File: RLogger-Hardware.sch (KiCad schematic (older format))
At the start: 13 parts

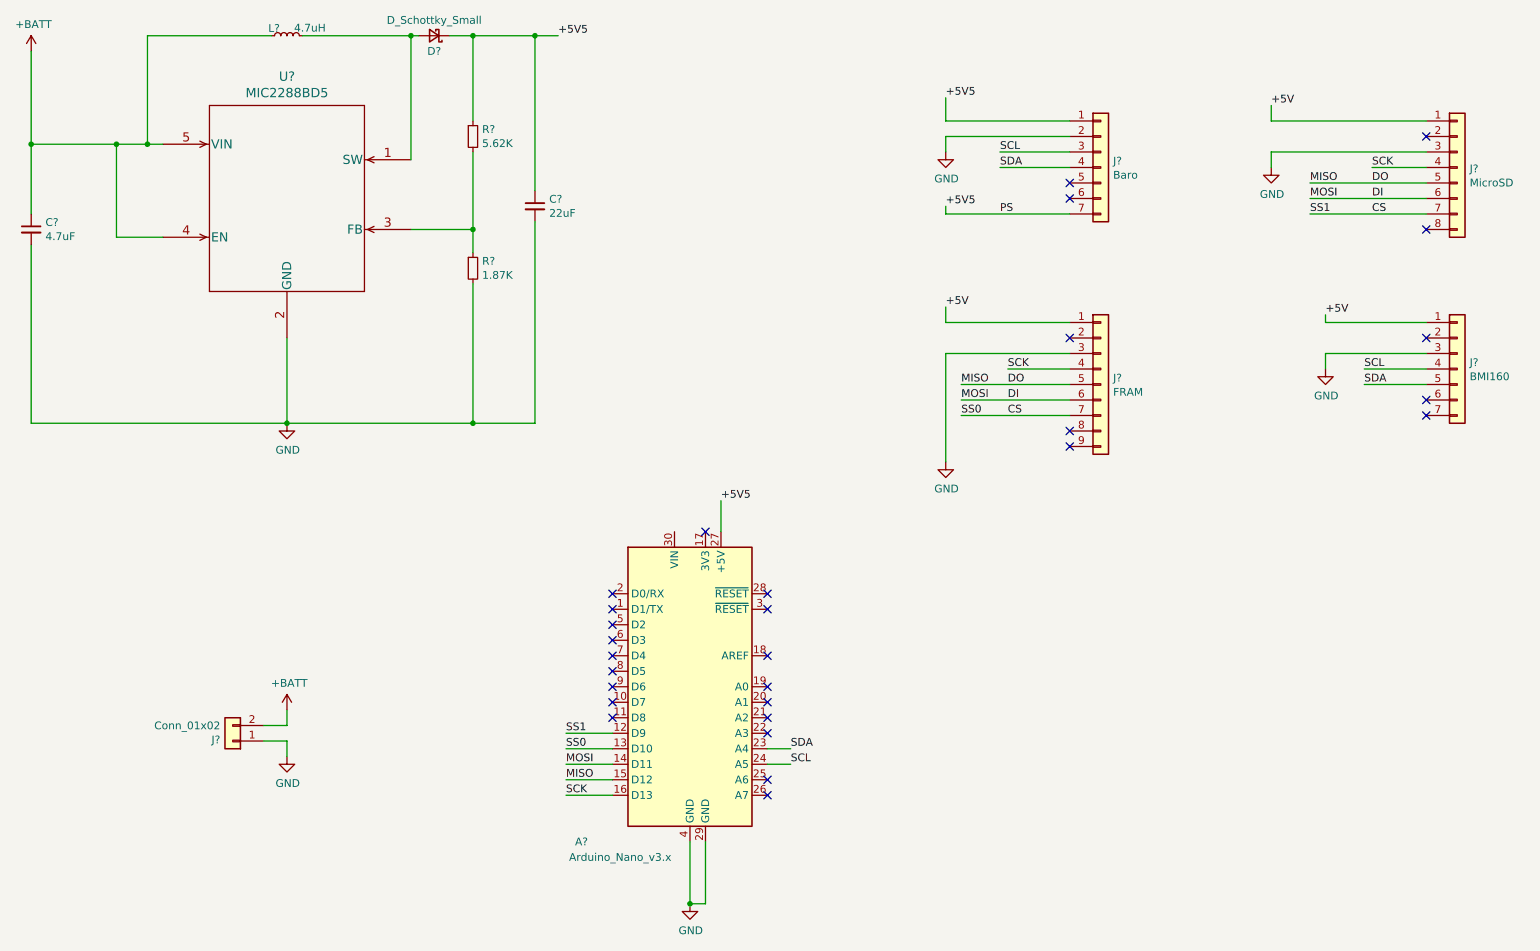
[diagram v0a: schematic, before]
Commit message: Assigned footprints.
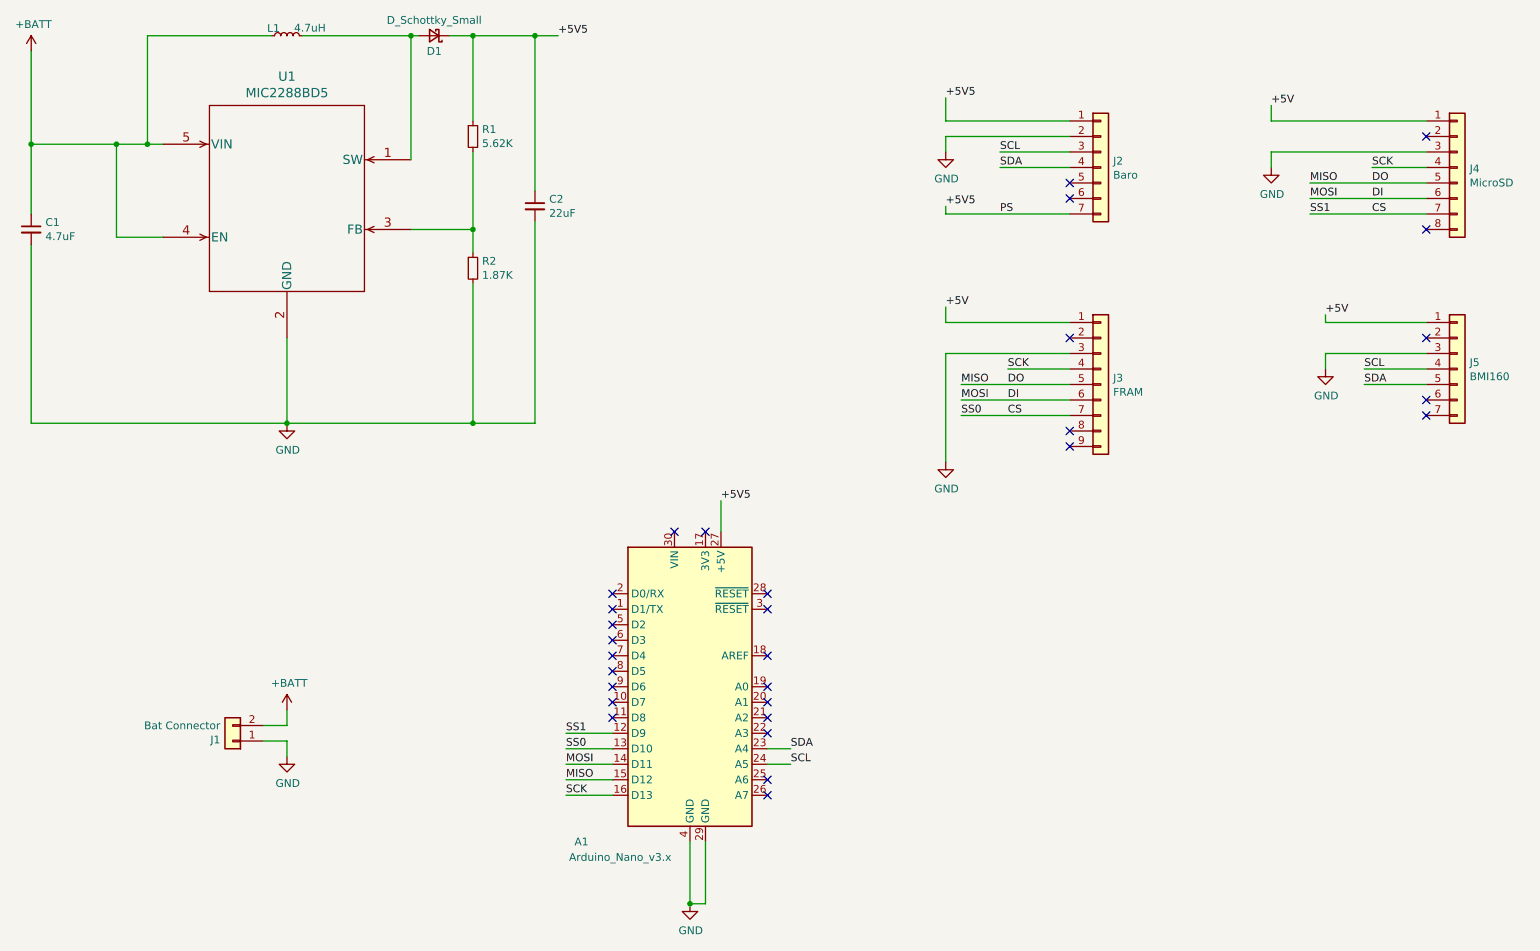
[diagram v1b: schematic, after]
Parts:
- C1: renamed from C?; footprint (none) -> Capacitor_SMD:C_0805_2012Metric_Pad1.15x1.40mm_HandSolder
- C2: renamed from C?; footprint (none) -> Capacitor_SMD:C_1206_3216Metric_Pad1.33x1.80mm_HandSolder
- D1: renamed from D?; footprint (none) -> Diode_SMD:D_Powermite_AK
- J1: renamed from J?; value Conn_01x02 -> Bat Connector; footprint (none) -> Connector_PinSocket_2.54mm:PinSocket_1x02_P2.54mm_Vertical
- J2, J5: renamed from J?; footprint (none) -> Connector_PinSocket_2.54mm:PinSocket_1x07_P2.54mm_Vertical
- J3: renamed from J?; footprint (none) -> Connector_PinSocket_2.54mm:PinSocket_1x09_P2.54mm_Vertical
- J4: renamed from J?; footprint (none) -> Connector_PinSocket_2.54mm:PinSocket_1x08_P2.54mm_Vertical
- L1: renamed from L?; footprint (none) -> Inductor_SMD:L_0805_2012Metric_Pad1.05x1.20mm_HandSolder
- R1, R2: renamed from R?; footprint (none) -> Resistor_SMD:R_0805_2012Metric_Pad1.15x1.40mm_HandSolder
- U1: renamed from U?; footprint TSOT-23-5_D5_MCL -> Package_TO_SOT_SMD:SOT-23-5_HandSoldering
- gave numbers to parts that had none: 1
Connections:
- no-connect marks 29 -> 30
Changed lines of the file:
@@
 $EndDescr
 $Comp
-L MCU_Module:Arduino_Nano_v3.x A?
+L MCU_Module:Arduino_Nano_v3.x A1
 U 1 1 6083FCEE
 P 5150 5000
-F 0 "A?" H 4450 4000 50  0000 C CNN
+F 0 "A1" H 4450 4000 50  0000 C CNN
 F 1 "Arduino_Nano_v3.x" H 4700 3900 50  0000 C CNN
 F 2 "Module:Arduino_Nano" H 5150 5000 50  0001 C CIN
@@
 $EndComp
 $Comp
-L Connector_Generic:Conn_01x08 J?
+L Connector_Generic:Conn_01x08 J4
 U 1 1 60843AEA
 P 10100 1650
-F 0 "J?" H 10180 1642 50  0000 L CNN
+F 0 "J4" H 10180 1642 50  0000 L CNN
 F 1 "MicroSD" H 10180 1551 50  0000 L CNN
-F 2 "" H 10100 1650 50  0001 C CNN
+F 2 "Connector_PinSocket_2.54mm:PinSocket_1x08_P2.54mm_Vertical" H 10100 1650 50  0001 C CNN
 F 3 "~" H 10100 1650 50  0001 C CNN
 	1    10100 1650
@@
 $EndComp
 $Comp
-L Connector_Generic:Conn_01x07 J?
+L Connector_Generic:Conn_01x07 J5
 U 1 1 6084440D
 P 10100 2950
-F 0 "J?" H 10180 2992 50  0000 L CNN
+F 0 "J5" H 10180 2992 50  0000 L CNN
 F 1 "BMI160" H 10180 2901 50  0000 L CNN
-F 2 "" H 10100 2950 50  0001 C CNN
+F 2 "Connector_PinSocket_2.54mm:PinSocket_1x07_P2.54mm_Vertical" H 10100 2950 50  0001 C CNN
 F 3 "~" H 10100 2950 50  0001 C CNN
 	1    10100 2950
@@
 $EndComp
 $Comp
-L Connector_Generic:Conn_01x07 J?
+L Connector_Generic:Conn_01x07 J2
 U 1 1 60844CC8
 P 7800 1650
-F 0 "J?" H 7880 1692 50  0000 L CNN
+F 0 "J2" H 7880 1692 50  0000 L CNN
 F 1 "Baro" H 7880 1601 50  0000 L CNN
-F 2 "" H 7800 1650 50  0001 C CNN
+F 2 "Connector_PinSocket_2.54mm:PinSocket_1x07_P2.54mm_Vertical" H 7800 1650 50  0001 C CNN
 F 3 "~" H 7800 1650 50  0001 C CNN
 	1    7800 1650
@@
 $EndComp
 $Comp
-L Connector_Generic:Conn_01x09 J?
+L Connector_Generic:Conn_01x09 J3
 U 1 1 60845B10
 P 7800 3050
-F 0 "J?" H 7880 3092 50  0000 L CNN
+F 0 "J3" H 7880 3092 50  0000 L CNN
 F 1 "FRAM" H 7880 3001 50  0000 L CNN
-F 2 "" H 7800 3050 50  0001 C CNN
+F 2 "Connector_PinSocket_2.54mm:PinSocket_1x09_P2.54mm_Vertical" H 7800 3050 50  0001 C CNN
 F 3 "~" H 7800 3050 50  0001 C CNN
 	1    7800 3050
@@
 	7150 1550 7600 1550
 $Comp
-L power:GND #PWR?
+L power:GND #PWR06
 U 1 1 6085614E
 P 6800 1550
-F 0 "#PWR?" H 6800 1300 50  0001 C CNN
+F 0 "#PWR06" H 6800 1300 50  0001 C CNN
 F 1 "GND" H 6805 1377 50  0000 C CNN
 F 2 "" H 6800 1550 50  0001 C CNN
@@
 	9900 1650 9550 1650
 $Comp
-L power:GND #PWR?
+L power:GND #PWR08
 U 1 1 60857E73
 P 8900 1650
-F 0 "#PWR?" H 8900 1400 50  0001 C CNN
+F 0 "#PWR08" H 8900 1400 50  0001 C CNN
 F 1 "GND" H 8905 1477 50  0000 C CNN
 F 2 "" H 8900 1650 50  0001 C CNN
@@
 	7600 2950 7200 2950
 $Comp
-L power:GND #PWR?
+L power:GND #PWR07
 U 1 1 6085AAD2
 P 6800 3550
-F 0 "#PWR?" H 6800 3300 50  0001 C CNN
+F 0 "#PWR07" H 6800 3300 50  0001 C CNN
 F 1 "GND" H 6805 3377 50  0000 C CNN
 F 2 "" H 6800 3550 50  0001 C CNN
@@
 	9900 2950 9500 2950
 $Comp
-L power:GND #PWR?
+L power:GND #PWR09
 U 1 1 6085E93A
 P 9250 2950
-F 0 "#PWR?" H 9250 2700 50  0001 C CNN
+F 0 "#PWR09" H 9250 2700 50  0001 C CNN
 F 1 "GND" H 9255 2777 50  0000 C CNN
 F 2 "" H 9250 2950 50  0001 C CNN
@@
 NoConn ~ 5250 4000
 $Comp
-L power:GND #PWR?
+L power:GND #PWR05
 U 1 1 60935326
 P 5150 6400
-F 0 "#PWR?" H 5150 6150 50  0001 C CNN
+F 0 "#PWR05" H 5150 6150 50  0001 C CNN
 F 1 "GND" H 5155 6227 50  0000 C CNN
 F 2 "" H 5150 6400 50  0001 C CNN
@@
 	5350 4000 5350 3800
 $Comp
-L Device:C_Small C?
+L Device:C_Small C2
 U 1 1 6093AD85
 P 4150 1900
-F 0 "C?" H 4242 1946 50  0000 L CNN
+F 0 "C2" H 4242 1946 50  0000 L CNN
 F 1 "22uF" H 4242 1855 50  0000 L CNN
-F 2 "" H 4150 1900 50  0001 C CNN
+F 2 "Capacitor_SMD:C_1206_3216Metric_Pad1.33x1.80mm_HandSolder" H 4150 1900 50  0001 C CNN
 F 3 "~" H 4150 1900 50  0001 C CNN
 	1    4150 1900
@@
 $EndComp
 $Comp
-L Device:R_Small R?
+L Device:R_Small R2
 U 1 1 6093C05F
 P 3750 2300
-F 0 "R?" H 3809 2346 50  0000 L CNN
+F 0 "R2" H 3809 2346 50  0000 L CNN
 F 1 "1.87K" H 3809 2255 50  0000 L CNN
-F 2 "" H 3750 2300 50  0001 C CNN
+F 2 "Resistor_SMD:R_0805_2012Metric_Pad1.15x1.40mm_HandSolder" H 3750 2300 50  0001 C CNN
 F 3 "~" H 3750 2300 50  0001 C CNN
 	1    3750 2300
@@
 $EndComp
 $Comp
-L Device:R_Small R?
+L Device:R_Small R1
 U 1 1 6093C433
 P 3750 1450
-F 0 "R?" H 3809 1496 50  0000 L CNN
+F 0 "R1" H 3809 1496 50  0000 L CNN
 F 1 "5.62K" H 3809 1405 50  0000 L CNN
-F 2 "" H 3750 1450 50  0001 C CNN
+F 2 "Resistor_SMD:R_0805_2012Metric_Pad1.15x1.40mm_HandSolder" H 3750 1450 50  0001 C CNN
 F 3 "~" H 3750 1450 50  0001 C CNN
 	1    3750 1450
@@
 $EndComp
 $Comp
-L Device:L_Small L?
+L Device:L_Small L1
 U 1 1 6093D259
 P 2550 800
-F 0 "L?" V 2598 846 50  0000 L CNN
+F 0 "L1" V 2598 846 50  0000 L CNN
 F 1 "4.7uH" V 2600 550 50  0000 L CNN
-F 2 "" H 2550 800 50  0001 C CNN
+F 2 "Inductor_SMD:L_0805_2012Metric_Pad1.05x1.20mm_HandSolder" H 2550 800 50  0001 C CNN
 F 3 "~" H 2550 800 50  0001 C CNN
 	1    2550 800
@@
 $EndComp
 $Comp
-L Device:D_Schottky_Small D?
+L Device:D_Schottky_Small D1
 U 1 1 6093DFC5
 P 3500 800
-F 0 "D?" H 3500 900 50  0000 C CNN
+F 0 "D1" H 3500 900 50  0000 C CNN
 F 1 "D_Schottky_Small" H 3500 700 50  0000 C CNN
-F 2 "" V 3500 800 50  0001 C CNN
+F 2 "Diode_SMD:D_Powermite_AK" V 3500 800 50  0001 C CNN
 F 3 "~" V 3500 800 50  0001 C CNN
 	1    3500 800
@@
 $EndComp
 $Comp
-L Connector_Generic:Conn_01x02 J?
+L Connector_Generic:Conn_01x02 J1
 U 1 1 609558EB
 P 2200 5350
-F 0 "J?" H 2280 5342 50  0000 L CNN
-F 1 "Conn_01x02" H 2280 5251 50  0000 L CNN
-F 2 "" H 2200 5350 50  0001 C CNN
+F 0 "J1" H 2280 5342 50  0000 L CNN
+F 1 "Bat Connector" H 2280 5251 50  0000 L CNN
+F 2 "Connector_PinSocket_2.54mm:PinSocket_1x02_P2.54mm_Vertical" H 2200 5350 50  0001 C CNN
 F 3 "~" H 2200 5350 50  0001 C CNN
 	1    2200 5350
@@
 $EndComp
 $Comp
-L power:GND #PWR?
+L power:GND #PWR04
 U 1 1 60957449
 P 2550 5450
-F 0 "#PWR?" H 2550 5200 50  0001 C CNN
+F 0 "#PWR04" H 2550 5200 50  0001 C CNN
 F 1 "GND" H 2555 5277 50  0000 C CNN
 F 2 "" H 2550 5450 50  0001 C CNN
@@
 $EndComp
 $Comp
-L power:+BATT #PWR?
+L power:+BATT #PWR03
 U 1 1 60957E11
 P 2550 5150
-F 0 "#PWR?" H 2550 5000 50  0001 C CNN
+F 0 "#PWR03" H 2550 5000 50  0001 C CNN
 F 1 "+BATT" H 2565 5323 50  0000 C CNN
 F 2 "" H 2550 5150 50  0001 C CNN
@@
 	2550 5350 2550 5450
 $Comp
-L MIC2288BD5:MIC2288BD5 U?
+L MIC2288BD5:MIC2288BD5 U1
 U 1 1 60993818
 P 2550 1850
-F 0 "U?" H 2550 2637 60  0000 C CNN
+F 0 "U1" H 2550 2637 60  0000 C CNN
 F 1 "MIC2288BD5" H 2550 2531 60  0000 C CNN
-F 2 "TSOT-23-5_D5_MCL" H 2550 2490 60  0001 C CNN
+F 2 "Package_TO_SOT_SMD:SOT-23-5_HandSoldering" H 2550 2490 60  0001 C CNN
 F 3 "http://www.farnell.com/datasheets/1670780.pdf" H 2550 2531 60  0001 C CNN
 	1    2550 1850
@@
 $EndComp
 $Comp
-L power:+BATT #PWR?
+L power:+BATT #PWR01
 U 1 1 609971C3
 P 900 900
-F 0 "#PWR?" H 900 750 50  0001 C CNN
+F 0 "#PWR01" H 900 750 50  0001 C CNN
 F 1 "+BATT" H 915 1073 50  0000 C CNN
 F 2 "" H 900 900 50  0001 C CNN
@@
 	900  1500 1450 1500
 $Comp
-L power:GND #PWR?
+L power:GND #PWR02
 U 1 1 60998F3D
 P 2550 3300
-F 0 "#PWR?" H 2550 3050 50  0001 C CNN
+F 0 "#PWR02" H 2550 3050 50  0001 C CNN
 F 1 "GND" H 2555 3127 50  0000 C CNN
 F 2 "" H 2550 3300 50  0001 C CNN
@@
 	2550 3300 2550 2750
 $Comp
-L Device:C_Small C?
+L Device:C_Small C1
 U 1 1 6099B342
 P 900 2050
-F 0 "C?" H 992 2096 50  0000 L CNN
+F 0 "C1" H 992 2096 50  0000 L CNN
 F 1 "4.7uF" H 992 2005 50  0000 L CNN
-F 2 "" H 900 2050 50  0001 C CNN
+F 2 "Capacitor_SMD:C_0805_2012Metric_Pad1.15x1.40mm_HandSolder" H 900 2050 50  0001 C CNN
 F 3 "~" H 900 2050 50  0001 C CNN
 	1    900  2050
@@
 Wire Wire Line
 	3750 2050 3750 1550
+NoConn ~ 5050 4000
 $EndSCHEMATC

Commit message: PCB done :o
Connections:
- net +5V5 is gone; now on net +5V: A1.27 (+5V), C2.1, D1.1 (K), J2.1 (Pin_1), J2.7 (Pin_7), R1.1
- net CS renamed SS0
- net SS0: no longer A1.12 (D9), J4.7 (Pin_7)
- new net SS1: A1.12 (D9), J4.7 (Pin_7)
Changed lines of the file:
@@
 Text Label 9550 1850 0    50   ~ 0
 DI
-Text Label 9550 1950 0    50   ~ 0
-CS
 Text Label 6800 2550 0    50   ~ 0
 +5V
@@
 Text Label 7200 3150 0    50   ~ 0
 DI
-Text Label 7200 3250 0    50   ~ 0
-CS
 Text Label 9250 2600 0    50   ~ 0
 +5V
@@
 	5800 5500 5650 5500
 Text Label 6800 1900 0    50   ~ 0
-+5V5
++5V
 Wire Wire Line
 	6800 1950 6800 1900
@@
 Text Label 6900 3250 0    50   ~ 0
 SS0
-Wire Wire Line
-	6900 3250 7600 3250
 NoConn ~ 9900 2750
 Text Label 9150 1750 0    50   ~ 0
@@
 Text Label 9150 1950 0    50   ~ 0
 SS1
-Wire Wire Line
-	9150 1950 9900 1950
 Wire Wire Line
 	9150 1850 9900 1850
@@
 Connection ~ 5150 6400
 Text Label 6800 1200 0    50   ~ 0
-+5V5
++5V
 Text Label 5350 3800 0    50   ~ 0
-+5V5
++5V
 Wire Wire Line
 	5350 4000 5350 3800
@@
 	3350 800  3400 800
 Text Label 4300 800  0    50   ~ 0
-+5V5
++5V
 Wire Wire Line
 	3600 800  3750 800
@@
 	3750 2050 3750 1550
 NoConn ~ 5050 4000
+Wire Wire Line
+	7600 3250 6900 3250
+Wire Wire Line
+	9900 1950 9150 1950
 $EndSCHEMATC

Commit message: Added mounting holes. Updated PCB layout. Generated fabrication files.
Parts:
- added H1, H2: MountingHole, MountingHole:MountingHole_2.2mm_M2, symbol Mechanical:MountingHole
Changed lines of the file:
@@
 Wire Wire Line
 	9900 1950 9150 1950
+$Comp
+L Mechanical:MountingHole H1
+U 1 1 60931938
+P 7400 5200
+F 0 "H1" H 7500 5246 50  0000 L CNN
+F 1 "MountingHole" H 7500 5155 50  0000 L CNN
+F 2 "MountingHole:MountingHole_2.2mm_M2" H 7500 5109 50  0001 L CNN
+F 3 "~" H 7400 5200 50  0001 C CNN
+	1    7400 5200
+	1    0    0    -1
+$EndComp
+$Comp
+L Mechanical:MountingHole H2
+U 1 1 609352AC
+P 7400 5400
+F 0 "H2" H 7500 5446 50  0000 L CNN
+F 1 "MountingHole" H 7500 5355 50  0000 L CNN
+F 2 "MountingHole:MountingHole_2.2mm_M2" H 7500 5309 50  0001 L CNN
+F 3 "~" H 7400 5400 50  0001 C CNN
+	1    7400 5400
+	1    0    0    -1
+$EndComp
 $EndSCHEMATC
